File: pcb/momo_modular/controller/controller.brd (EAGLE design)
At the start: 50.8 x 33 mm, 52 parts, among them Q1 MOSFET-N, Q2 P-MOSFET, U1 VOLTAGE-SUPERVISOR-BD45312, U2 PIC24FJ64GA306, U3 MCP1702, U4 RN4020_BT_4.0_MODULE, U5 FLASH8MSOP8, U6 MCP73811, U7 TS1102-CURRENT-SENSE

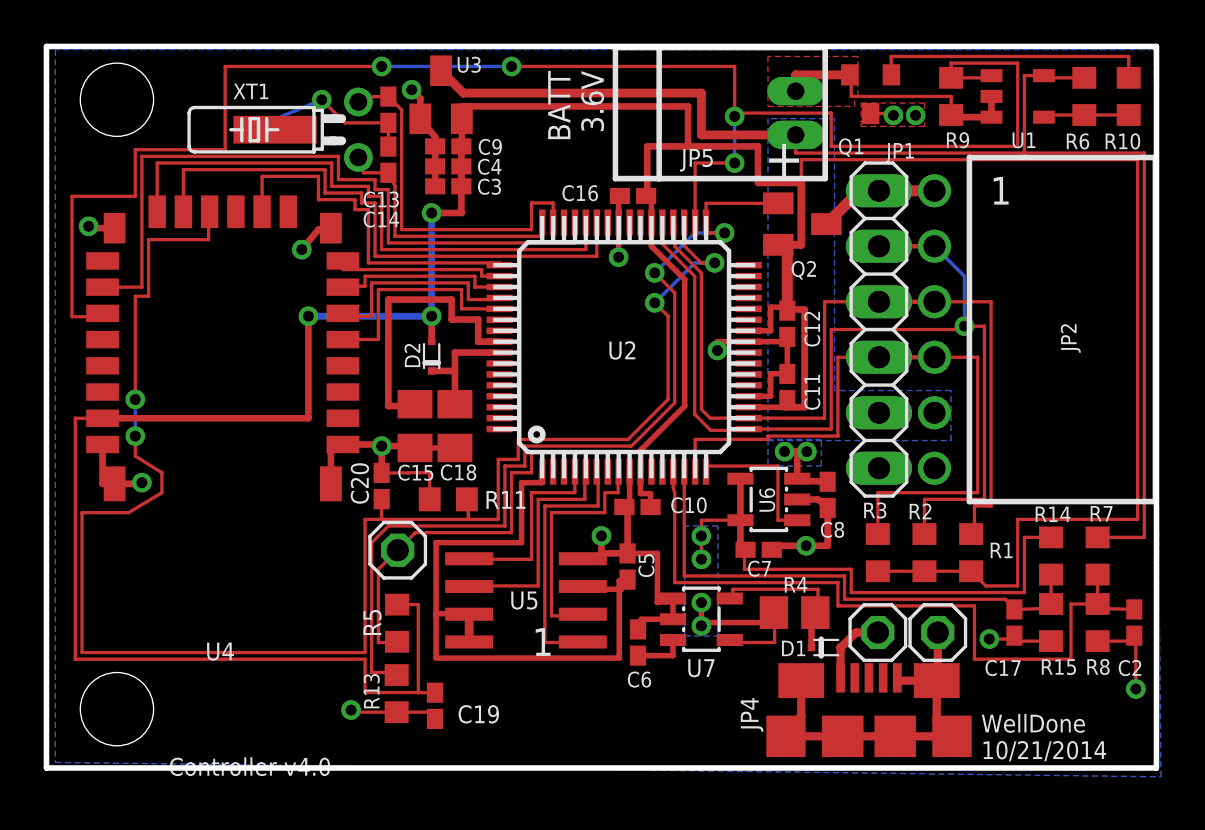
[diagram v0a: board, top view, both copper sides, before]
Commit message: Merge pull request #141 from timburke/pr-controller-v4
Update Controller Hardware to Version 4.0

Update controller board to rev 4.0.

- New version contains BTLE via Microchip RN4020 module
- Voltage supervisor with hard reset capability from bluetooth
or via microcontroller
- Current monitor for solar and external charging current
- Move 2.8V linear regulator and add RF filtering caps to fix RF
interference problems on GSM transmission.

Merge pull request #141 from timburke/pr-controller-v4

Update Controller Hardware to Version 4.0

Update controller board to rev 4.0.

- New version contains BTLE via Microchip RN4020 module
- Voltage supervisor with hard reset capability from bluetooth
or via microcontroller
- Current monitor for solar and external charging current
- Move 2.8V linear regulator and add RF filtering caps to fix RF
interference problems on GSM transmission.

Rename combined_controller to controller

We don't have different assembly variants anymore so the
combined isn't needed.

Update controller board to version 4.1

- Fix parasitic path through hw reset controller by passing control
signal through an optocoupler
- Replace Li-ion battery charger IC with constant current regulator
to allow for solar panel charging
- Add solar panel current measurement with 1 ohm shunt and differential
ADC lines

Fix battery charging and simplify reset circuit.

- Remove MOSFET from battery- to minimize R on GSM power supply
- Add constant current charger for charging from external source
- Update parts to compatible versions with lower cost D1-3, Q2,4

Update part sizing document.

Update HW Reset components for increased reliability based on SPICE

- larger RC network on discharge FET.
- increased required assert time to 120 ms.
- reset pulse length: ~100 ms @ 25C

Rename controller board from combined_controller

Update controller project file.

Remove autorouter file.

Update labeling on schematic

Add spice models for controller battery charging and hw reset

U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
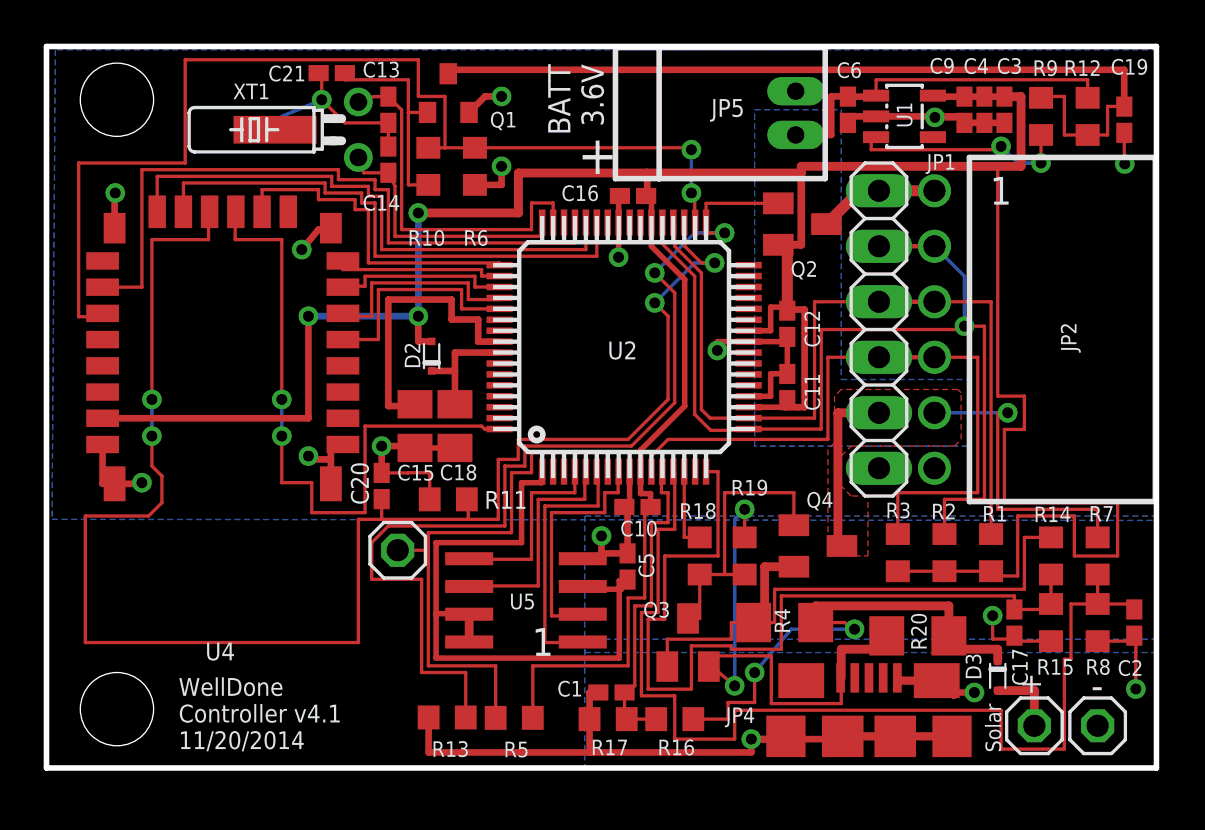
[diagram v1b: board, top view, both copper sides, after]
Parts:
- removed C7: 1 uF, rcl:C0402K
- removed C8: 1uF, rcl:C0402K
- removed D1: (no value), diode:SC79_INFINEON
- removed U3: MCP1702, components:SOT23
- removed U6: MCP73811, components:SOT23-5L
- removed U7: TS1102-CURRENT-SENSE, custom_ics:SOT23-5L
- added C1: 100 nF, rcl:C0402K
- added C21: 1 uF, rcl:C0402K
- added D3: (no value), diode:SC79_INFINEON
- added Q3: (no value), transistor-pnp:SOT23
- added Q4: P-MOSFET, components:SOT23
- added R12, R16, R17: 510K, rcl:R0603
- added R18: 10K, rcl:R0603
- added R19: 100K, rcl:R0603
- added R20: 1 ohm, rcl:R1206
- C19: value 22 pF -> 1 uF
- C6: value 47 nF -> 1 uF
- R10: value 100R -> 100K
- R4: value 51 mOhms -> 1 ohm; device rcl:R0805 -> rcl:R1206
- R9: value 100K -> 10K
- U1: value VOLTAGE-SUPERVISOR-BD45312 -> XC6504-LINEAR-REGULATOR; device custom_ics:SSOP-5 -> custom_ics:SOT23-5L
- moved C19 41.4 mm to (83.4, 41.6)
- moved R10 32.2 mm to (51.5, 39.5), turned to 90 degrees
- moved R6 28.1 mm to (53.6, 39.5), turned to 90 degrees
- moved C6 26.2 mm to (70.7, 42.1), turned to 270 degrees
- moved C3 25.7 mm to (77.9, 42.1), turned to 270 degrees
- moved C4 24.7 mm to (77.0, 42.1), turned to 270 degrees
- moved C9 23.7 mm to (76.0, 42.1), turned to 270 degrees
- moved Q1 19.3 mm to (52.4, 42.8), turned to 0 degrees
- moved JP7 8.47 mm to (82.1, 13.9)
- moved JP8 8.34 mm to (79.2, 13.9)
- moved R5 6.89 mm to (55.4, 14.2), turned to 0 degrees
- moved U1 5.26 mm to (73.3, 41.8), turned to 270 degrees
- moved R9 4.22 mm to (79.6, 41.8)
- moved R13 2.56 mm to (52.4, 14.2), turned to 0 degrees
- moved R1 0.91 mm to (77.3, 21.8)
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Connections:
- removed net +5V: C7.1, R14.2, R4.2, U6.4, U6.5, U7.4
- removed net CHG_CURR: C6.1, U7.3
- removed net N$8: R10.2, R6.2, U1.4
- removed net N$9: D1.A, JP4.1, JP8.1
- removed net RS+: D1.C, R4.1, U7.5
- removed net VEXT_SAMP: C17.1, R14.1, R15.2, U2.14
- new net CHG_I+: D3.C, R16.2, R20.2, R4.1
- new net CHG_I-: Q3.1, Q4.2, R14.2, R4.2
- new net N$10: Q3.3, Q4.1, R18.2, R19.1
- new net N$11: C19.1, Q1.3, R12.1, R9.2
- new net N$2: C21.1, Q1.1, R10.1
- new net N$3: D3.A, JP8.1
- new net PIO3: U2.64, U4.PIO3
- new net SAMP_CHG+: C1.1, R16.1, R17.2, U2.12
- new net SAMP_CHG-: C17.1, R14.1, R15.2, U2.16
- net CHG_EN: now also R18.1, U2.14; no longer U2.16, U6.1
- net GND: now also C1.2, C21.2, JP5.2, Q1.2, R17.1, R6.1, U1.2; no longer C7.2, C8.2, JP4.GND1, Q1.3, U3.1, U6.2, U7.1, U7.2
- net HW_RESET: now also R10.2, R6.2; no longer R9.2, U1.1
- net IRQ: now also U2.11; no longer U2.15
- net N$1: now also R9.1, U1.3; no longer Q1.1, R10.1
- net N$5: now also JP4.1, Q3.2, R19.2, R20.1; no longer JP5.2, Q1.2, R9.1, U1.2, U1.3
- net V+: now also C6.1, Q4.3, R12.2, U1.1; no longer C8.1, R6.1, U1.5, U3.3, U6.3
- net VCCINT: now also U1.5; no longer C19.1, U3.2
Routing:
- net N$11: track 0.00 -> 39.8 mm
- net SAMP_CHG-: track 0.00 -> 38.9 mm
- net +5V: track 33.6 -> 0.00 mm, vias 4 -> 0
- net PIO3: track 0.00 -> 29.9 mm, vias 0 -> 2
- net CHG_I-: track 0.00 -> 27.4 mm
- net HW_RESET: track 76.4 -> 49.3 mm, vias 4 -> 2
- net V+: track 65.2 -> 39.3 mm, vias 2 -> 1
- net VEXT_SAMP: track 24.4 -> 0.00 mm
- net CHG_I+: track 0.00 -> 23.9 mm, vias 0 -> 2
- net VCCINT: track 175.0 -> 155.1 mm
- net SAMP_CHG+: track 0.00 -> 14.8 mm
- net VBAT_SAMP: track 33.7 -> 47.9 mm
- net N$10: track 0.00 -> 13.4 mm
- net N$5: track 12.6 -> 24.9 mm, vias 0 -> 2
- net GND: track 93.1 -> 105.0 mm, vias 15 -> 17
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- added copper zone on layer 1, net V+
- removed copper zone on layer 16, net +5V
- removed copper zone on layer 1, net GND
- removed copper zone on layer 1, net N$5
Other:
- board text added: "Solar"
- board text added: "WellDone Controller v4.1 11/20/2014"
- board text removed: "Controller v4.0"
- board text removed: "WellDone 10/21/2014"

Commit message: Update controller to v4.2
- Try to fix RF feedback issue using ferrite beads
- Add 100 uF tantalum output cap for better load stability
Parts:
- removed C18: 10 uF, rcl:C0805K
- removed C19, C21: 1 uF, rcl:C0402K
- removed C20: 22 pF, rcl:C0402K
- removed C4: 10 pF, rcl:C0402K
- removed D2: (no value), diode:SC79_INFINEON
- removed Q1: MOSFET-N, custom_ics:SOT-23
- removed R10, R11, R6: 100K, rcl:R0603
- removed R12: 510K, rcl:R0603
- removed R9: 10K, rcl:R0603
- added FB1, FB2: (no value), rcl:R0603
- C3: value 33 pF -> 100 uF; device rcl:C0402K -> rcl:B/3528-21R
- moved C3 4.15 mm to (81.8, 43.3), turned to 180 degrees
- moved C6 2.66 mm to (73.3, 42.7)
- moved C9 2.66 mm to (78.6, 42.7)
- moved U1 2.66 mm to (75.9, 42.4)
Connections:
- removed net HW_RESET: R10.2, R6.2, U2.34, U4.PIO7
- removed net N$11: C19.1, Q1.3, R12.1, R9.2
- removed net PIO4: C20.1, R11.2, U2.35, U4.PIO4
- removed net VBAT: C18.1, D2.C, U2.57
- net CONN: now also U2.35
- net GND: now also C3.-; no longer C18.2, C19.2, C20.2, C21.2, C3.2, C4.2, Q1.2, R11.1, R6.1
- net N$1: now also C3.+, C9.1, FB2.1, U1.5; no longer R9.1, U1.3
- net N$2: now also C6.1, FB1.2, U1.1, U1.3; no longer C21.1, Q1.1, R10.1
- net V+: now also FB1.1; no longer C6.1, R12.2, U1.1
- net VCCINT: now also FB2.2, U2.57; no longer C3.1, C4.1, C9.1, D2.A, U1.5
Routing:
- net PIO4: track 75.2 -> 0.00 mm, vias 4 -> 0
- net HW_RESET: track 49.3 -> 0.00 mm, vias 2 -> 0
- net N$11: track 39.8 -> 0.00 mm
- net CONN: track 0.00 -> 28.7 mm, vias 0 -> 4
- net V+: track 39.3 -> 26.0 mm
- net GND: track 105.0 -> 99.2 mm, vias 17 -> 15
- net VBAT: track 5.47 -> 0.00 mm
- net N$1: track 10.3 -> 6.29 mm, vias 2 -> 0
- net N$2: track 9.82 -> 7.62 mm
- net VCCINT: track 155.1 -> 156.9 mm
- net N$6: track 16.8 -> 18.4 mm
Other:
- board text added: "WellDone Controller v4.2 7/28/2015"
- board text removed: "WellDone Controller v4.1 11/20/2014"
